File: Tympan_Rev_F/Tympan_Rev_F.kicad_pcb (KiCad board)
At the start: 4 copper layers, 38 x 74 mm, 91 parts, among them J1 SJ-3523-SMT-TR, J2 SJ-3524-SMT-TR-PI, J3 Conn_01x06, J4 Qwiik Connector, J7 J-Link, P1 CONN_01X06, P2 CONN_01X06, P3 CONN_01X06, P4 CONN_01X06, P6 CONN_01X01, P7 CONN_01X01, P8 CONN_01X01, SW1 CL-SB-22A, SW2 SW_Push, U1 MCP73831, U2 TLV320AIC3206IRSBT, U3 74LVC1G66, U4 LP5907MFX-1.8, U5 Teensy4.1, U6 LC709203, U7 MDBT50Q-1MV2, Y1 32.768

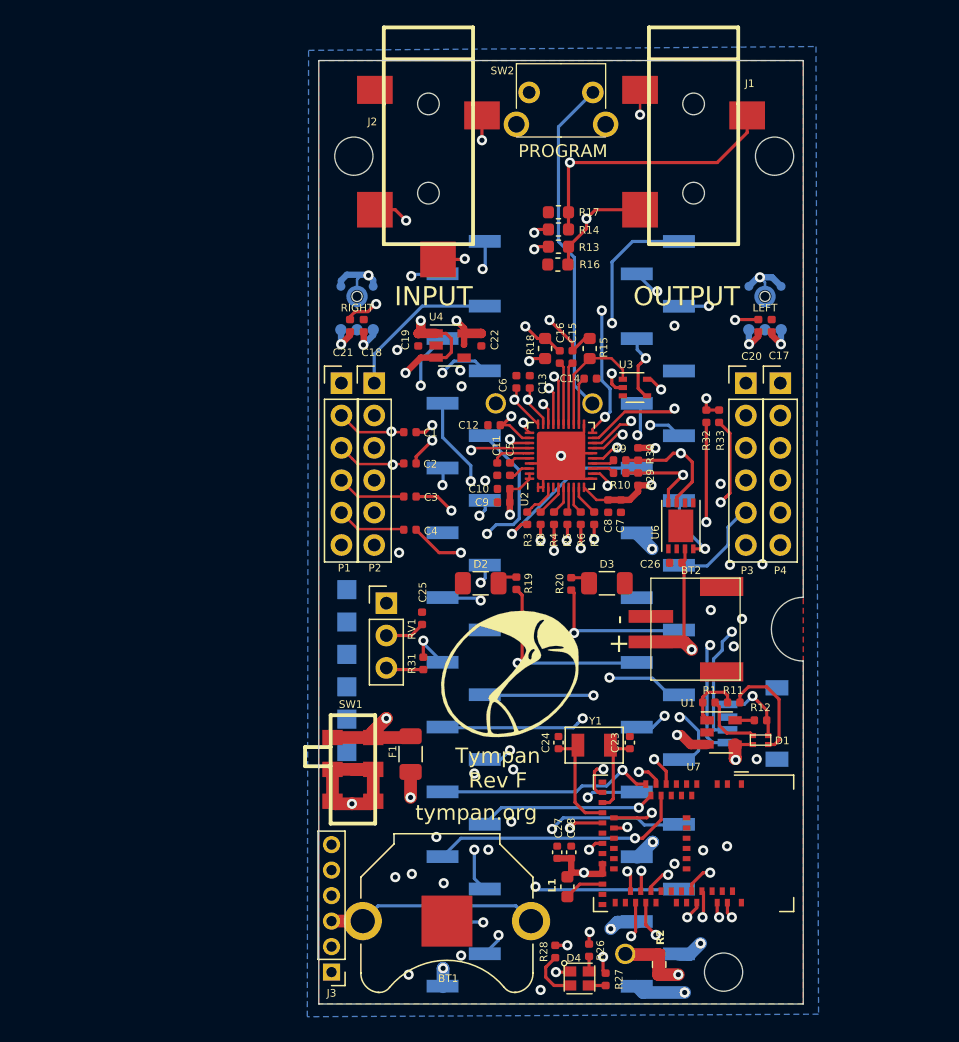
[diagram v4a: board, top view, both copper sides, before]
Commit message: Passing DRC Getting ready for production
Added a file for the nRF52 radio module programmer. This will use pogo pins.
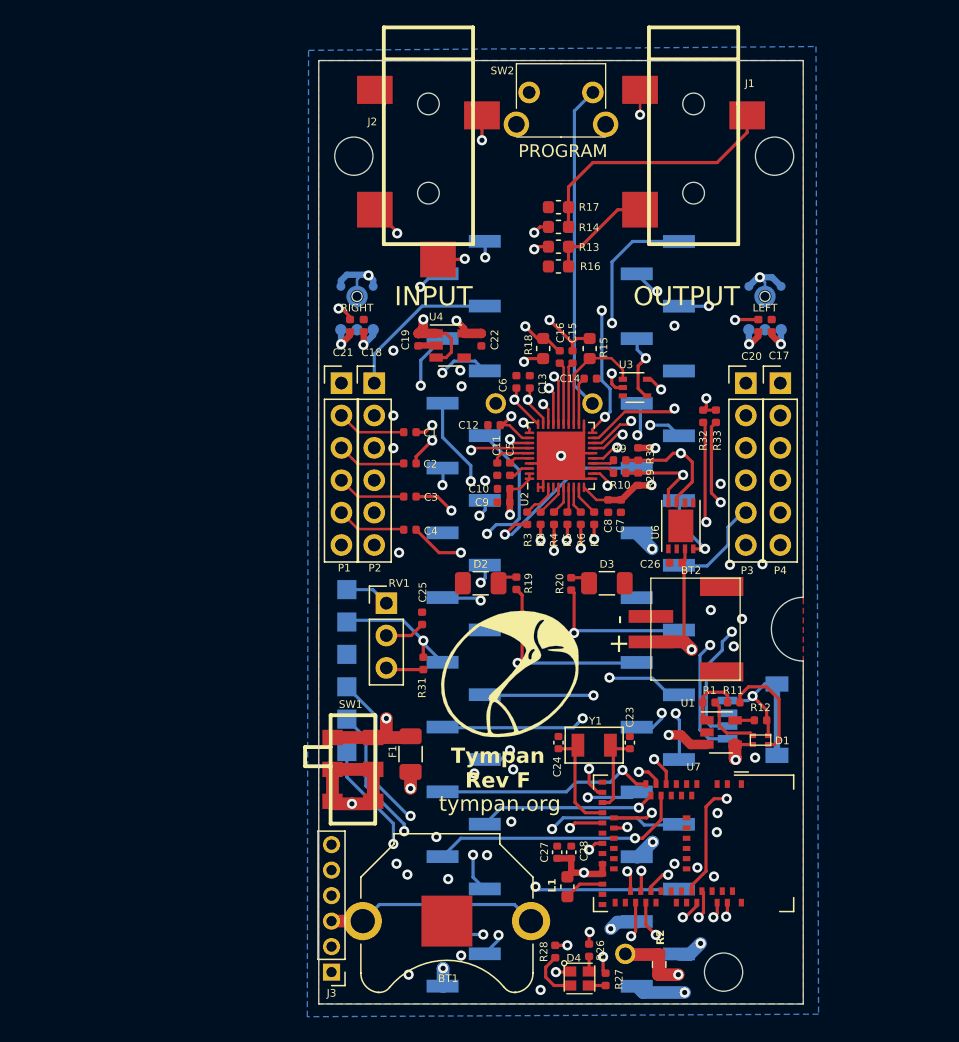
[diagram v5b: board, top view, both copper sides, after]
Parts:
- moved R17 0.40 mm to (153.2, 70.7)
- moved J4 0.30 mm to (168.4, 110.9)
- moved R32 0.25 mm to (164.6, 87.1)
- moved R33 0.25 mm to (165.6, 87.1)
- moved R14 0.20 mm to (153.2, 72.2)
- moved R16 0.16 mm to (153.2, 75.3)
- moved R18 0.15 mm to (152.0, 81.8)
- moved G*** 0.10 mm to (153.5, 68.7)
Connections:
- BT2 pad 3: (no net) -> GND
- BT2 pad 4: (no net) -> GND
- J4 pad : (no net) -> GND
- SW2 pad 3: (no net) -> GND
- SW2 pad 4: (no net) -> GND
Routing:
- net /SWCLK: track 1.29 -> 47.3 mm, vias 1 -> 3
- net /SWO: track 2.37 -> 47.8 mm, vias 1 -> 2
- net /SWDIO: track 1.21 -> 45.3 mm, vias 1 -> 3
- net GND: track 71.2 -> 82.5 mm
- net /BT_nRESET: track 60.5 -> 66.9 mm
- net /BT_TX: track 72.9 -> 69.5 mm
- net /35_TX8: track 82.8 -> 85.6 mm
- net /V_BAT: track 57.9 -> 60.5 mm
- net /34_RX8: track 82.5 -> 84.8 mm
- net +BATT: track 60.5 -> 58.9 mm
- net /IN2_R: track 31.1 -> 32.5 mm
- net /MCLK: track 60.5 -> 61.9 mm
- net Net-(J2-T): track 31.1 -> 29.8 mm
- net /SCL: track 31.6 -> 30.4 mm
- net /R: track 21.5 -> 20.3 mm, vias 1 -> 0
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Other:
- rule pad_to_mask_clearance: 0.051 -> 0

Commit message: Production Files Approved
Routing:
- net /DOUT_1: track 50.5 -> 48.0 mm
- net /34_RX8: track 84.8 -> 86.5 mm
- net /V_USB: track 8.25 -> 9.44 mm
- net /BT_TX: track 69.5 -> 70.3 mm, vias 4 -> 3
- net /35_TX8: track 85.6 -> 86.1 mm
